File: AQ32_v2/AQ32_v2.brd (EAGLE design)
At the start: 57.1 x 57.1 mm, 115 parts, among them Q2 BCV27, Q3 BCV27, Q5 BCV27, Q6 BCV27, U1 ITG-3200, U10 MS5611, U11 MIC5239, U13 74AHC1G86DCK, U2 STM32F10XVXT6, U7 USD-SOCKETNEW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

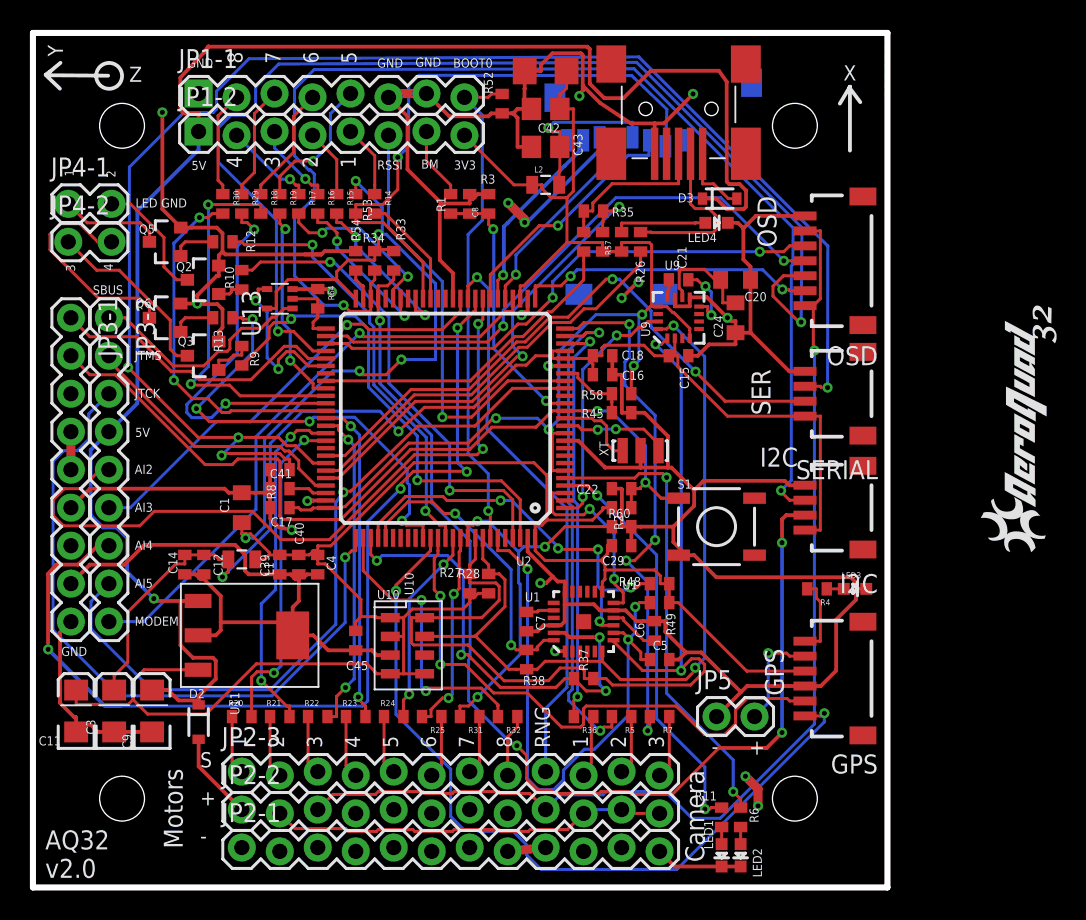
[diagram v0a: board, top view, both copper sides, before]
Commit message: Beefed up +5V in and ground traces
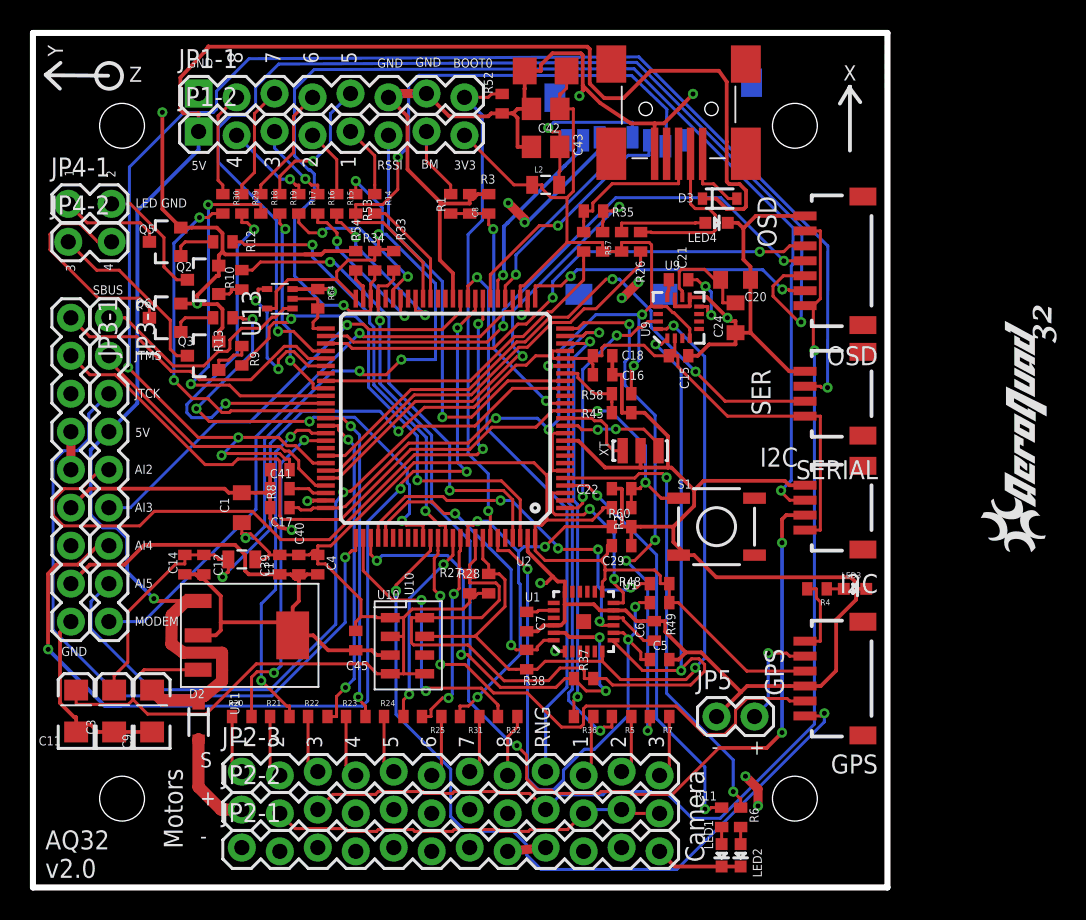
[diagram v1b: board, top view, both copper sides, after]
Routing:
- net 5VIN: track 111.1 -> 113.2 mm
- net 5V-1: track 5.90 -> 6.72 mm
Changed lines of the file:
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@@
 <wire x1="9.8665" y1="19.16" x2="8.2439" y2="19.16" width="0.254" layer="1"/>
 <wire x1="8.2439" y1="19.16" x2="8.0858" y2="19.3181" width="0.254" layer="1"/>
-<wire x1="10.4563" y1="19.16" x2="9.8665" y2="19.16" width="0.254" layer="1"/>
+<wire x1="10.4563" y1="19.16" x2="10.25" y2="19.16" width="0.254" layer="1"/>
+<wire x1="10.25" y1="19.16" x2="9.8665" y2="19.16" width="0.254" layer="1"/>
 <wire x1="11.046" y1="19.16" x2="10.4563" y2="19.16" width="0.254" layer="1"/>
 <wire x1="11.08" y1="50.557" x2="11.08" y2="51.7763" width="0.254" layer="1"/>
@@
 <wire x1="46.3924" y1="45.3754" x2="45.6978" y2="46.07" width="0.254" layer="1"/>
 <wire x1="45.6978" y1="46.07" x2="44.78" y2="46.07" width="0.254" layer="1"/>
-<wire x1="7.97" y1="13.2" x2="9.0495" y2="13.2" width="0.254" layer="1"/>
-<wire x1="11.08" y1="12.5073" x2="9.7422" y2="12.5073" width="0.254" layer="1"/>
-<wire x1="9.7422" y1="12.5073" x2="9.0495" y2="13.2" width="0.254" layer="1"/>
 <wire x1="11.08" y1="12.5073" x2="11.08" y2="12.8045" width="0.254" layer="1"/>
 <wire x1="11.08" y1="12.21" x2="11.08" y2="12.5073" width="0.254" layer="1"/>
-<wire x1="9.8665" y1="19.16" x2="9.8665" y2="16.1937" width="0.254" layer="1"/>
-<wire x1="9.8665" y1="16.1937" x2="10.6974" y2="15.3628" width="0.254" layer="1"/>
-<wire x1="10.6974" y1="15.3628" x2="12.0346" y2="15.3628" width="0.254" layer="1"/>
-<wire x1="12.0346" y1="15.3628" x2="12.2256" y2="15.1718" width="0.254" layer="1"/>
-<wire x1="12.2256" y1="15.1718" x2="12.2256" y2="13.9501" width="0.254" layer="1"/>
-<wire x1="12.2256" y1="13.9501" x2="11.08" y2="12.8045" width="0.254" layer="1"/>
 <wire x1="45.8796" y1="54.6194" x2="41.3194" y2="54.6194" width="0.254" layer="1"/>
 <wire x1="41.3194" y1="54.6194" x2="39.49" y2="52.79" width="0.254" layer="1"/>
@@
 <wire x1="37.08" y1="56.23" x2="11.749109375" y2="56.23" width="0.254" layer="1"/>
 <wire x1="11.749109375" y1="56.23" x2="11.729509375" y2="56.2496" width="0.254" layer="1"/>
+<wire x1="11.08" y1="12.5073" x2="8.6627" y2="12.5073" width="0.8128" layer="1"/>
+<wire x1="8.6627" y1="12.5073" x2="7.97" y2="13.2" width="0.8128" layer="1"/>
+<wire x1="11.08" y1="12.8045" x2="11.4545" y2="12.8045" width="0.8128" layer="1"/>
+<wire x1="11.4545" y1="12.8045" x2="12.65" y2="13.79" width="0.8128" layer="1"/>
+<wire x1="12.65" y1="13.79" x2="12.65" y2="14.53" width="0.8128" layer="1"/>
+<wire x1="12.65" y1="14.53" x2="12.65" y2="15.7" width="0.8128" layer="1"/>
+<wire x1="12.65" y1="15.7" x2="10.06" y2="15.7" width="0.8128" layer="1"/>
+<wire x1="10.06" y1="15.7" x2="9.26" y2="16.28" width="0.8128" layer="1"/>
+<wire x1="9.26" y1="16.28" x2="9.28" y2="18.22" width="0.8128" layer="1"/>
+<wire x1="9.28" y1="18.22" x2="10.25" y2="19.16" width="0.8128" layer="1"/>
 </signal>
 <signal name="LED1">
@@
 <via x="39.3759" y="39.42" extent="1-16" drill="0.3302" diameter="0.6858"/>
 <via x="40.4959" y="40.48" extent="1-16" drill="0.3302" diameter="0.6858"/>
-<wire x1="40.4959" y1="40.48" x2="40.4359" y2="40.48" width="0.254" layer="1"/>
-<wire x1="40.4359" y1="40.48" x2="39.3759" y2="39.42" width="0.254" layer="1"/>
 <via x="44.1459" y="53.07" extent="1-16" drill="0.3302" diameter="0.6858"/>
 <wire x1="41.58" y1="51.0995" x2="42.2095" y2="51.0995" width="0.254" layer="1"/>
@@
 <wire x1="36.7696" y1="53.6277" x2="36.7696" y2="53.4004" width="0.254" layer="1"/>
 <wire x1="36.7696" y1="53.4004" x2="36.83" y2="53.34" width="0.254" layer="1"/>
+<wire x1="39.3759" y1="39.42" x2="39.4359" y2="39.42" width="0.6096" layer="1"/>
+<wire x1="39.4359" y1="39.42" x2="40.4959" y2="40.48" width="0.6096" layer="1"/>
 </signal>
 <signal name="PE10">
@@
 <contactref element="JP2-2" pad="1"/>
 <contactref element="D2" pad="2"/>
-<wire x1="13.97" y1="5.207" x2="11.08" y2="8.097" width="0.254" layer="1"/>
-<wire x1="11.08" y1="8.097" x2="11.08" y2="9.91" width="0.254" layer="1"/>
+<wire x1="13.97" y1="5.207" x2="12.583" y2="5.207" width="0.8128" layer="1"/>
+<wire x1="12.583" y1="5.207" x2="11.07" y2="6.72" width="0.8128" layer="1"/>
+<wire x1="11.07" y1="6.72" x2="11.07" y2="9.9" width="0.8128" layer="1"/>
+<wire x1="11.07" y1="9.9" x2="11.08" y2="9.91" width="0.8128" layer="1"/>
 </signal>
 </signals>

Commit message: general route cleanup
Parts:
- moved U$4 46.8 mm to (25.8, 40.9), flipped to the bottom, turned to 0 degrees
- moved U$5 24.2 mm to (19.6, 14.4)
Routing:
- net GND: track 321.8 -> 323.3 mm
- net 5VIN: track 113.2 -> 111.9 mm
- net N$9: track 2.94 -> 2.24 mm
- net UART1_RX: track 103.1 -> 102.5 mm

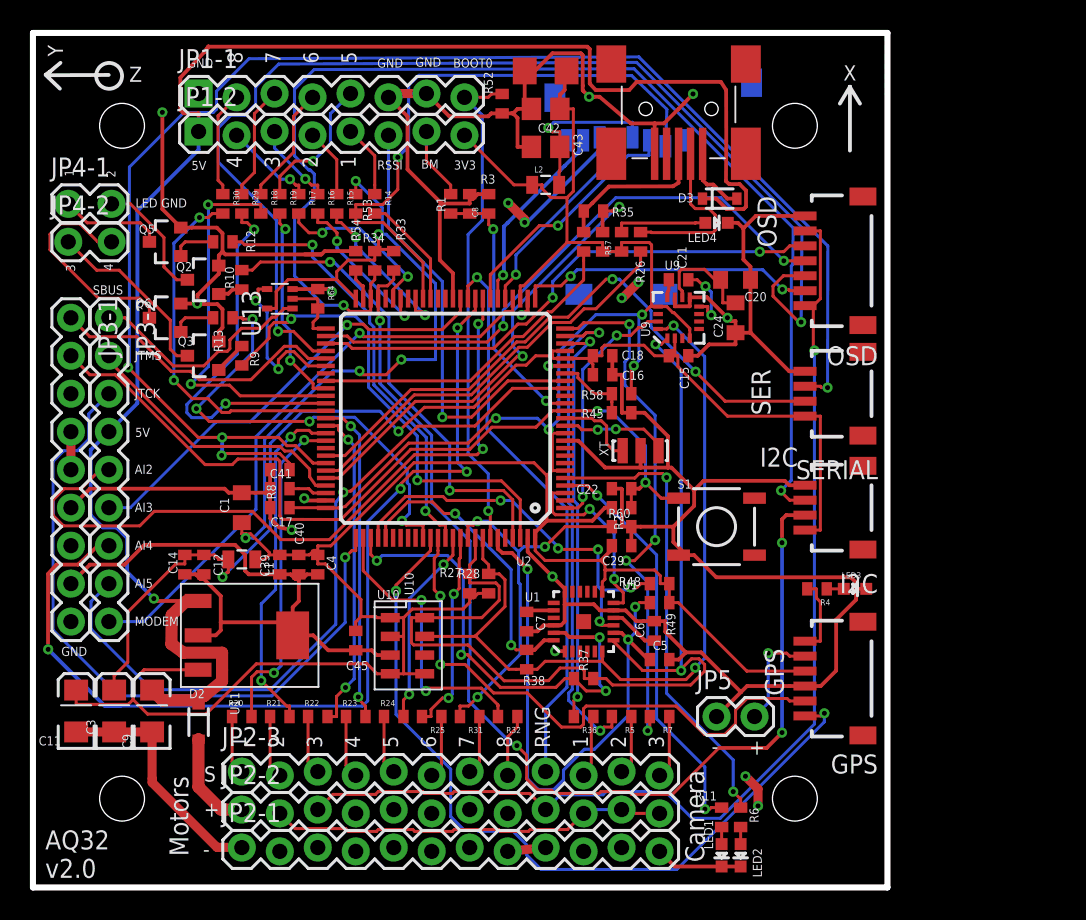
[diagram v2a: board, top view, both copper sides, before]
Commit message: relocated BM input away from 3.3V input, added more clearance between mounting holes and USB input, added XOR gate to SBUS TX, added ground plane to top side of board
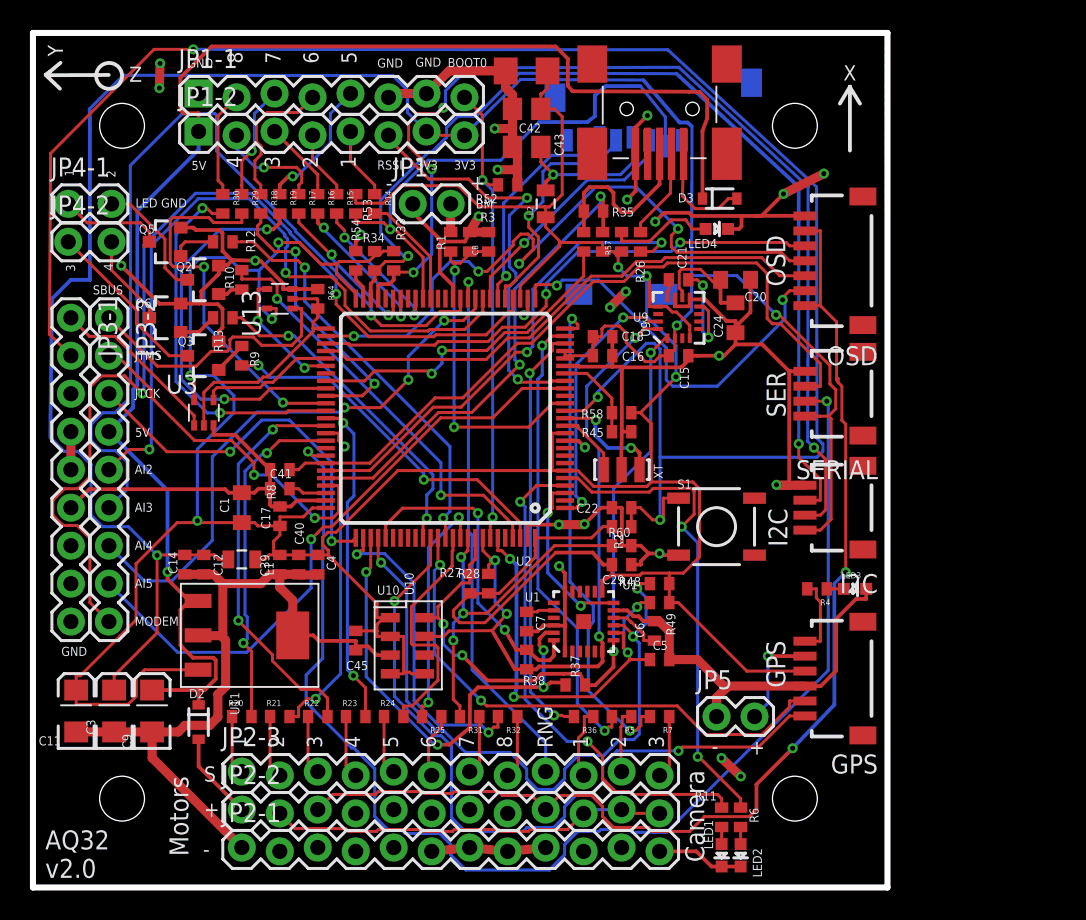
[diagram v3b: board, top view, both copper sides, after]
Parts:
- added JP1: (no value), SparkFun-Connectors:1X02
- added U3: 74AHC1G86DCK, 74xx-little-us:SC70-5
- moved R52 5.44 mm to (31.8, 47.0), turned to 180 degrees
- moved C8 2.54 mm to (30.5, 43.2)
- moved R1 2.54 mm to (27.9, 43.2)
- moved R3 2.54 mm to (29.2, 43.2)
- moved XT 1.80 mm to (39.4, 27.9), turned to 180 degrees
- moved C16 1.27 mm to (38.1, 35.6)
- moved C22 1.27 mm to (39.4, 25.4)
- moved L2 1.27 mm to (34.3, 45.7), turned to 90 degrees
- moved R58 1.27 mm to (39.4, 31.8)
- moved X2 1.27 mm to (41.9, 52.1)
- moved C29 1.27 mm to (39.4, 21.6)
- moved R2 1.27 mm to (39.4, 24.1)
- moved R45 1.27 mm to (39.4, 30.5)
- moved R60 1.27 mm to (39.4, 22.9)
- moved C18 1.27 mm to (38.1, 36.8)
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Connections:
- new net PD8: U2.55, U3.4
- net 3V3AN: now also JP1-2.7, JP1-2.8
- net 3V3DIG: now also U3.5; no longer JP1-2.8
- net GND: now also JP1.1, U3.3
- net LIPO: now also JP1.2; no longer JP1-2.7
- net NSS2_LV: now also U3.2
- net UART3_TX: now also U3.1; no longer U2.55
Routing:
- net JTAG-TRST: track 56.9 -> 126.8 mm, vias 2 -> 3
- net 3V3AN: track 81.7 -> 151.0 mm, vias 2 -> 3
- net UART1_RX: track 102.5 -> 48.3 mm, vias 4 -> 0
- net UART1_TX: track 40.9 -> 86.4 mm
- net MOSI2_LV: track 77.1 -> 35.6 mm, vias 2 -> 0
- net GND: track 323.3 -> 286.7 mm, vias 18 -> 25
- net TIM3_CH4: track 30.1 -> 59.0 mm
- net ADC12_IN15: track 65.6 -> 37.9 mm, vias 4 -> 3
- net NSS1_LV/DAC_OUT1: track 39.5 -> 66.3 mm, vias 1 -> 2
- net JTCK: track 47.4 -> 25.5 mm, vias 1 -> 2
- net SCL1_LV: track 67.9 -> 47.4 mm, vias 2 -> 4
- net MISO3_LV: track 27.4 -> 45.2 mm, vias 5 -> 3
- net SDA2_LV: track 80.7 -> 66.9 mm
- net TIM4_CH1: track 13.6 -> 26.4 mm
- net 5VIN: track 111.9 -> 99.5 mm
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- added copper zone on layer 1, net GND

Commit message: fixed SBUS Tx connection, fixed clearance issue with updated XOR connections, added extra vias for ground
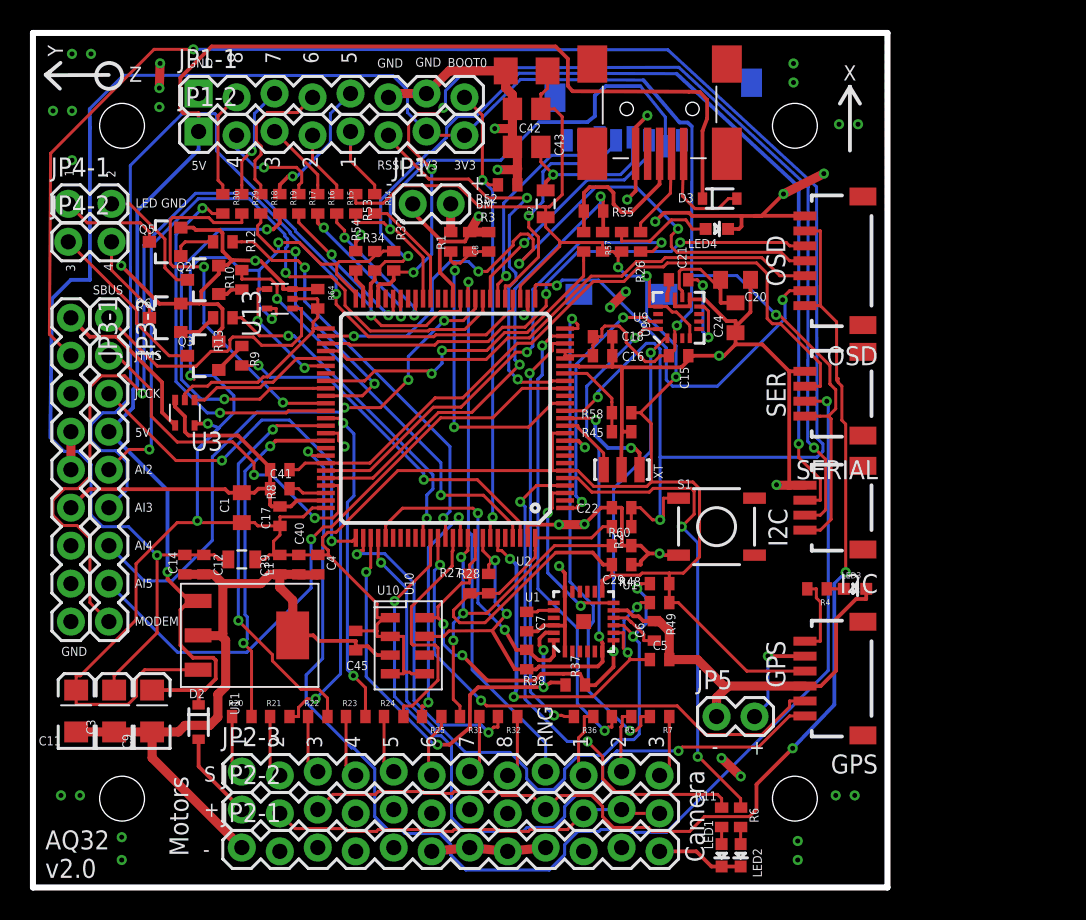
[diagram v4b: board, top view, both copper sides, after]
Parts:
- moved U3 1.27 mm to (10.2, 31.8), turned to 180 degrees
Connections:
- net PD8: now also U3.1; no longer U3.4
- net UART3_TX: now also U3.4; no longer U3.1
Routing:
- net GND: track 286.7 -> 289.8 mm, vias 25 -> 43
- net 3V3DIG: track 254.7 -> 257.1 mm, vias 7 -> 8
- net PD8: track 9.02 -> 9.93 mm
- net JTMS: track 23.4 -> 24.2 mm

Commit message: "j" version from Alfred
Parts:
- JP1: value (none) -> JP1; device SparkFun-Connectors:1X02 -> SparkFun-Connectors:1X02_LOCK
- moved JP1 20.2 mm to (5.21, 45.9), turned to 180 degrees
- moved C8 19.8 mm to (11.2, 47.6), turned to 270 degrees
- moved R3 19.7 mm to (10.0, 47.6), turned to 90 degrees
- moved R1 19.6 mm to (8.83, 47.6), turned to 270 degrees
- moved R53 7.62 mm to (29.1, 46.7), turned to 90 degrees
- moved XT 3.35 mm to (38.3, 31.1), turned to 270 degrees
- moved R45 3.21 mm to (40.7, 33.4)
- moved JP4-1 2.42 mm to (2.67, 43.3)
- moved JP4-2 2.42 mm to (2.67, 40.8)
- moved Q5 1.65 mm to (8.95, 44.8)
- moved C18 1.48 mm to (39.4, 36.1), turned to 270 degrees
- moved R58 1.39 mm to (40.7, 32.1)
- moved LED1 1.31 mm to (44.8, 2.47)
- moved R11 1.31 mm to (44.8, 5.01)
- moved LED2 1.31 mm to (46.1, 2.47)
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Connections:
- net 3V3AN: now also C29.1, C45.1, U1.13, U10.1, U10.2, U10.4, U10.5; no longer I2C.1, JP1-2.7, JP1-2.8, SERIAL.1
- net 3V3DIG: now also I2C.1, JP1-2.7, JP1-2.8, SERIAL.1; no longer C29.1, C45.1, U1.13, U10.1, U10.2, U10.4, U10.5
- net LEDGND1: now also Q2.3; no longer Q5.3
- net LEDGND2: now also Q5.3; no longer Q2.3
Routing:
- net 3V3AN: track 151.0 -> 88.2 mm, vias 3 -> 6
- net GND: track 289.8 -> 240.5 mm, vias 43 -> 90
- net 3V3DIG: track 257.1 -> 233.6 mm, vias 8 -> 9
- net ADC123_IN10: track 22.8 -> 43.3 mm
- net PE10: track 36.1 -> 29.5 mm, vias 1 -> 2
- net LIPO: track 1.89 -> 7.85 mm
- net LEDGND2: track 8.30 -> 2.93 mm
- net TIM4_CH3: track 25.0 -> 19.8 mm
- net NSS1_LV/DAC_OUT1: track 66.3 -> 71.2 mm
- net N$2: track 7.71 -> 3.09 mm, vias 2 -> 0
- net N$72: track 11.8 -> 8.00 mm
- net JTAG-TRST: track 126.8 -> 130.6 mm
- net SDA1_LV: track 47.6 -> 51.2 mm, vias 4 -> 2
- net SCK2_LV: track 45.4 -> 42.0 mm
- net TIM8_CH2: track 27.0 -> 30.1 mm
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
